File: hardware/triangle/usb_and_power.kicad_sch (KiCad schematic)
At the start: 15 parts, among them J1 USB_C_Receptacle_USB2.0_16P, J2 USB_C_Receptacle_USB2.0_16P, U2 EA8212HT6R

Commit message: trying to fix schematic
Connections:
- net -12V is gone; now on net +12V: C25.2, J1.A4 (VBUS), J1.A9 (VBUS), J1.B4 (VBUS), J1.B9 (VBUS), J2.A4 (VBUS), J2.A9 (VBUS), J2.B4 (VBUS), J2.B9 (VBUS)
- net +12V: now also C27.1, U2.5 (PWR)
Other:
- moved on the sheet: C25, C26, C27, C28, J2, L1, R3, R4, R7, R8, R9, U2

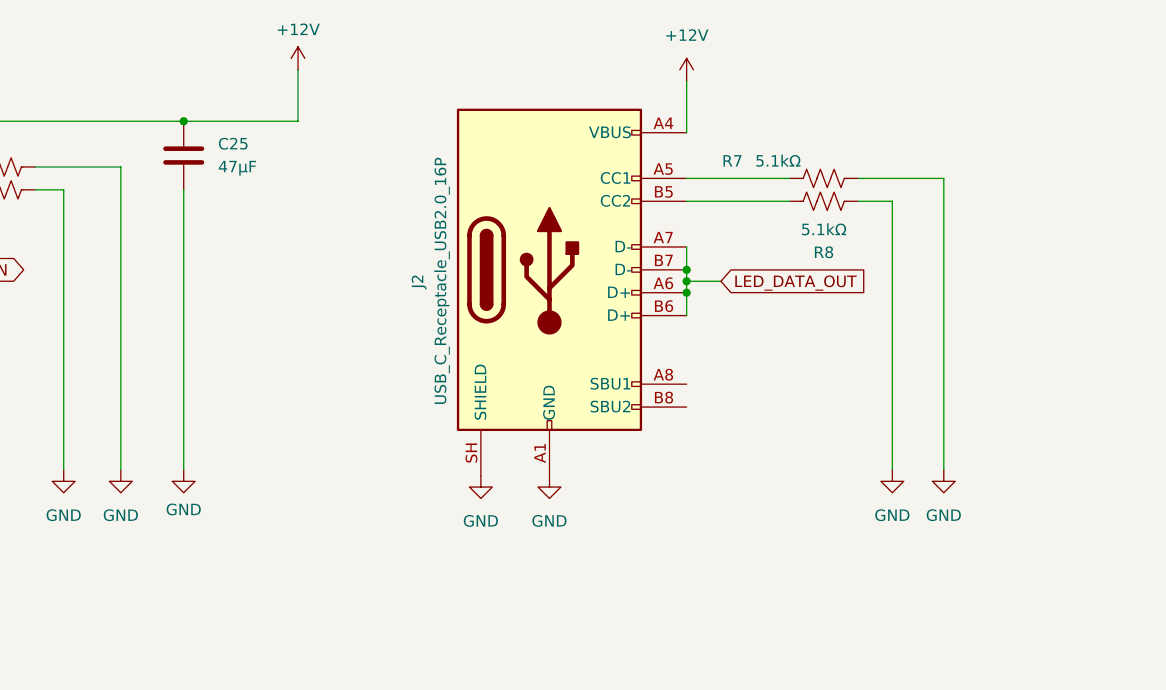
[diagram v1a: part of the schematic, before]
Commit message: add another capacitor
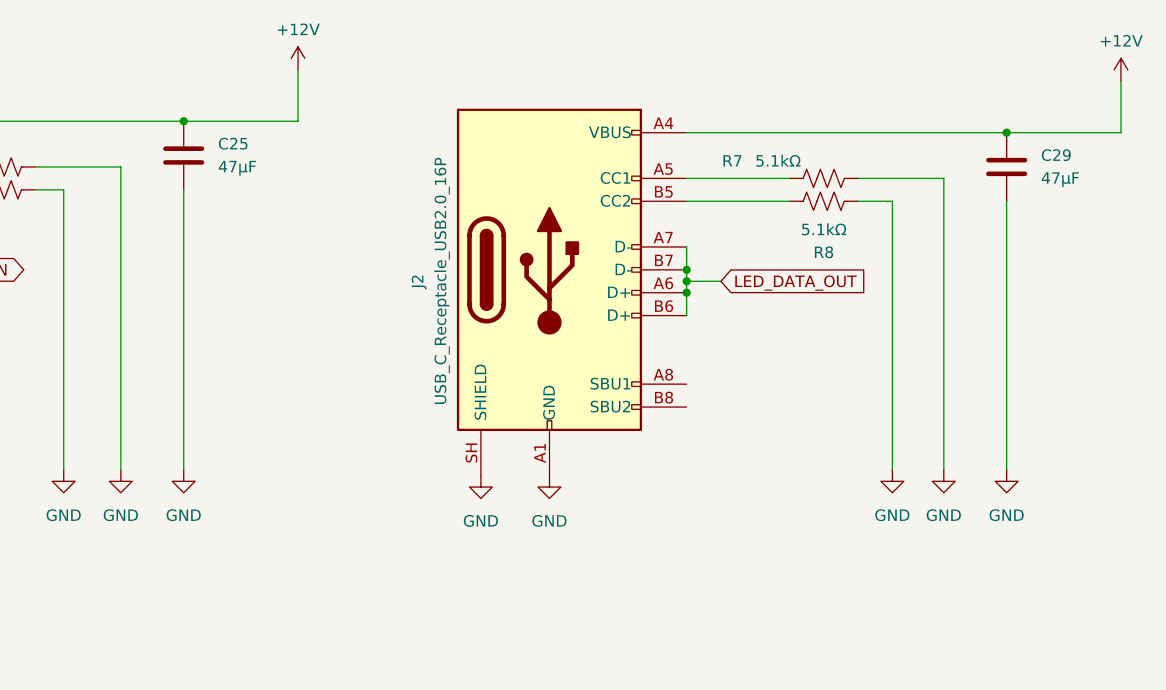
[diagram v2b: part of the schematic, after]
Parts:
- added C29: 47µF, Capacitor_SMD:C_1206_3216Metric, symbol Device:C
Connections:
- net +12V: now also C29.2
- net GND: now also C29.1
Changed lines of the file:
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@@
+	)
+	(junction
+		(at 198.12 44.45)
+		(diameter 0)
+		(color 0 0 0 0)
 	)
 	(junction
@@
 	(wire
 		(pts
+			(xy 198.12 81.915) (xy 198.12 52.07)
+		)
+		(stroke
+			(width 0)
+			(type default)
+		)
+	)
+	(wire
+		(pts
 			(xy 99.695 81.915) (xy 99.695 48.26)
 		)
@@
 	(wire
 		(pts
+			(xy 210.82 38.735) (xy 210.82 44.45)
+		)
+		(stroke
+			(width 0)
+			(type default)
+		)
+	)
+	(wire
+		(pts
 			(xy 104.775 168.91) (xy 104.775 164.465)
 		)
@@
 	(wire
 		(pts
-			(xy 162.56 44.45) (xy 162.56 38.735)
+			(xy 198.12 44.45) (xy 162.56 44.45)
 		)
 		(stroke
@@
 		(pts
 			(xy 76.835 140.97) (xy 76.835 149.86)
+		)
+		(stroke
+			(width 0)
+			(type default)
+		)
+	)
+	(wire
+		(pts
+			(xy 198.12 44.45) (xy 210.82 44.45)
 		)
 		(stroke
@@
 				)
 				(justify left)
+			)
+		)
+	)
+	(symbol
+		(lib_id "power:+12V")
+		(at 210.82 38.735 0)
+		(unit 1)
+		(body_style 1)
+		(exclude_from_sim no)
+		(in_bom yes)
+		(on_board yes)
+		(in_pos_files yes)
+		(dnp no)
+		(fields_autoplaced yes)
+		(property "Reference" "#PWR024"
+			(at 210.82 42.545 0)
+			(hide yes)
+			(show_name no)
+			(do_not_autoplace no)
+			(effects
+				(font
+					(size 1.27 1.27)
+				)
+			)
+		)
+		(property "Value" "+12V"
+			(at 210.82 34.29 0)
+			(show_name no)
+			(do_not_autoplace no)
+			(effects
+				(font
+					(size 1.27 1.27)
+				)
+			)
+		)
+		(property "Footprint" ""
+			(at 210.82 38.735 0)
+			(hide yes)
+			(show_name no)
+			(do_not_autoplace no)
+			(effects
+				(font
+					(size 1.27 1.27)
+				)
+			)
+		)
+		(property "Datasheet" ""
+			(at 210.82 38.735 0)
+			(hide yes)
+			(show_name no)
+			(do_not_autoplace no)
+			(effects
+				(font
+					(size 1.27 1.27)
+				)
+			)
+		)
+		(property "Description" "Power symbol creates a global label with name \"+12V\""
+			(at 210.82 38.735 0)
+			(hide yes)
+			(show_name no)
+			(do_not_autoplace no)
+			(effects
+				(font
+					(size 1.27 1.27)
+				)
+			)
+		)
+		(pin "1"
+		)
+		(instances
+			(project "triangle"
+				(path "/955e9dc0-fcd6-4d32-9a7f-93a0bda4c269"
+					(reference "#PWR024")
+					(unit 1)
+				)
 			)
 		)
@@
 	(symbol
 		(lib_id "power:+12V")
-		(at 162.56 38.735 0)
-		(unit 1)
-		(body_style 1)
-		(exclude_from_sim no)
-		(in_bom yes)
-		(on_board yes)
-		(in_pos_files yes)
-		(dnp no)
-		(fields_autoplaced yes)
-		(property "Reference" "#PWR016"
-			(at 162.56 42.545 0)
-			(hide yes)
-			(show_name no)
-			(do_not_autoplace no)
-			(effects
-				(font
-					(size 1.27 1.27)
-				)
-			)
-		)
-		(property "Value" "+12V"
-			(at 162.56 33.655 0)
-			(show_name no)
-			(do_not_autoplace no)
-			(effects
-				(font
-					(size 1.27 1.27)
-				)
-			)
-		)
-		(property "Footprint" ""
-			(at 162.56 38.735 0)
-			(hide yes)
-			(show_name no)
-			(do_not_autoplace no)
-			(effects
-				(font
-					(size 1.27 1.27)
-				)
-			)
-		)
-		(property "Datasheet" ""
-			(at 162.56 38.735 0)
-			(hide yes)
-			(show_name no)
-			(do_not_autoplace no)
-			(effects
-				(font
-					(size 1.27 1.27)
-				)
-			)
-		)
-		(property "Description" "Power symbol creates a global label with name \"+12V\""
-			(at 162.56 38.735 0)
-			(hide yes)
-			(show_name no)
-			(do_not_autoplace no)
-			(effects
-				(font
-					(size 1.27 1.27)
-				)
-			)
-		)
-		(pin "1"
-		)
-		(instances
-			(project "triangle"
-				(path "/955e9dc0-fcd6-4d32-9a7f-93a0bda4c269"
-					(reference "#PWR016")
-					(unit 1)
-				)
-			)
-		)
-	)
-	(symbol
-		(lib_id "power:+12V")
 		(at 142.875 113.665 0)
 		(unit 1)
@@
 	)
 	(symbol
+		(lib_id "Device:C")
+		(at 198.12 48.26 180)
+		(unit 1)
+		(body_style 1)
+		(exclude_from_sim no)
+		(in_bom yes)
+		(on_board yes)
+		(in_pos_files yes)
+		(dnp no)
+		(fields_autoplaced yes)
+		(property "Reference" "C29"
+			(at 201.93 46.9899 0)
+			(show_name no)
+			(do_not_autoplace no)
+			(effects
+				(font
+					(size 1.27 1.27)
+				)
+				(justify right)
+			)
+		)
+		(property "Value" "47µF"
+			(at 201.93 49.5299 0)
+			(show_name no)
+			(do_not_autoplace no)
+			(effects
+				(font
+					(size 1.27 1.27)
+				)
+				(justify right)
+			)
+		)
+		(property "Footprint" "Capacitor_SMD:C_1206_3216Metric"
+			(at 197.1548 44.45 0)
+			(hide yes)
+			(show_name no)
+			(do_not_autoplace no)
+			(effects
+				(font
+					(size 1.27 1.27)
+				)
+			)
+		)
+		(property "Datasheet" "https://jlc-prod-smt.oss-eu-central-1.aliyuncs.com/smtDataManualFile/8586178840691683328-C77101.pdf?response-content-disposition=attachment%3B%20filename%3DC77101.pdf%3B%20filename%2A%3DUTF-8%27%27C77101.pdf&x-oss-date=20260530T174020Z&x-oss-expires=1800&x-oss-security-token=CAISgAN1q6Ft5B2yfSjIr5n%2Bfdvem%2Bts05SjcVeCpXNkYt5rmo3Mrzz2IHhMdHJsAOodtv0%2FmmhT6PkclqRLcbhpcmfjV%2BZHzLB8qbk31zBO4J7b16cNrbH4M4H6aXeirtuwDsz9SNTCALjPD3nPii50x5bjaDymRCbLGJaViJlhHLN1Ow6jdmhpCctxLAlvo9NgFxm3D%2Fu2NQPwiWf9FVdhvhEG6Vly8qOi2MaRmFy8yFTx0b0SvJ%2BjYMrmPctoN9JnSdC5mfdzau3a1TJ84gRD0a5wkaVA1zbDs5bfISEIuUzebreLqY03dV4mOvdqIcMe8qigz88fk%2FfIioH6xyxKOexoSCnFTOiiupCcQLPyao9jLu6iayqViY7QaIOTqQohZmkAMwVOasAsI3Ngh4zF97Qt0cVNkXO9gWfLI8DtuMleWkppw9R5cnSgc5lCkRRYwGs1287ugXlSQzo890KPDAEovaKCnZ2ZSfh7Y4sNknI6i%2Bfc2Se2MIkIWjBNb6KWD5sagAGr5rmBvHeFC8TZ%2BJcd86gyYT9ErQ9X%2B0arh9aBqEUpMV00uZssw%2BpJ0wDNLR3IfY4Emrombd1Qhrr0MuB3K8fJjJk9FM3xSkdaC6wlZzPtmjTVgp5eXx0QJhMfflRGyQBUK%2FfqX4UcQ0%2FVp31Qo2ufdtTd4b5xoRPi6Re0vJceYCAA&x-oss-signature-version=OSS4-HMAC-SHA256&x-oss-credential=STS.NZK6ajv4MdVHsq3As1nQGuHgM%2F20260530%2Feu-central-1%2Foss%2Faliyun_v4_request&x-oss-signature=60c0d3c6bb64dcbae917457d6a6bcf0bef18835ea05f75f079bc953471331657"
+			(at 198.12 48.26 0)
+			(hide yes)
+			(show_name no)
+			(do_not_autoplace no)
+			(effects
+				(font
+					(size 1.27 1.27)
+				)
+			)
+		)
+		(property "Description" "Unpolarized capacitor"
+			(at 198.12 48.26 0)
+			(hide yes)
+			(show_name no)
+			(do_not_autoplace no)
+			(effects
+				(font
+					(size 1.27 1.27)
+				)
+			)
+		)
+		(property "JLCPCB Part #" "C77101"
+			(at 198.12 48.26 0)
+			(hide yes)
+			(show_name no)
+			(do_not_autoplace no)
+			(effects
+				(font
+					(size 1.27 1.27)
+				)
+			)
+		)
+		(pin "1"
+		)
+		(pin "2"
+		)
+		(instances
+			(project "triangle"
+				(path "/955e9dc0-fcd6-4d32-9a7f-93a0bda4c269"
+					(reference "C29")
+					(unit 1)
+				)
+			)
+		)
+	)
+	(symbol
 		(lib_id "Device:R_US")
 		(at 104.775 160.655 0)
@@
 		(in_pos_files yes)
 		(dnp no)
-		(fields_autoplaced yes)
 		(property "Reference" "#PWR02"
 			(at 106.68 88.265 0)
@@
 		)
 		(property "Value" "GND"
-			(at 106.68 86.36 0)
+			(at 106.68 86.995 0)
 			(show_name no)
 			(do_not_autoplace no)
@@
 					(unit 1)
 				)
+			)
+		)
+	)
+	(symbol
+		(lib_id "power:GND")
+		(at 198.12 81.915 0)
+		(unit 1)
+		(body_style 1)
+		(exclude_from_sim no)
+		(in_bom yes)
+		(on_board yes)
+		(in_pos_files yes)
+		(dnp no)
+		(property "Reference" "#PWR016"
+			(at 198.12 88.265 0)
+			(hide yes)
+			(show_name no)
+			(do_not_autoplace no)
+			(effects
+				(font
+					(size 1.27 1.27)
+				)
+			)
+		)
+		(property "Value" "GND"
+			(at 198.12 86.995 0)
+			(show_name no)
+			(do_not_autoplace no)
+			(effects
+				(font
+					(size 1.27 1.27)
+				)
+			)
+		)
+		(property "Footprint" ""
+			(at 198.12 81.915 0)
+			(hide yes)
+			(show_name no)
+			(do_not_autoplace no)
+			(effects
+				(font
+					(size 1.27 1.27)
+				)
+			)
+		)
+		(property "Datasheet" ""
+			(at 198.12 81.915 0)
+			(hide yes)
+			(show_name no)
+			(do_not_autoplace no)
+			(effects
+				(font
+					(size 1.27 1.27)
+				)
+			)
+		)
+		(property "Description" "Power symbol creates a global label with name \"GND\" , ground"
+			(at 198.12 81.915 0)
+			(hide yes)
+			(show_name no)
+			(do_not_autoplace no)
+			(effects
+				(font
+					(size 1.27 1.27)
+				)
+			)
+		)
+		(pin "1"
+		)
+		(instances
+			(project "triangle"
+				(path "/955e9dc0-fcd6-4d32-9a7f-93a0bda4c269"
+					(reference "#PWR016")
+					(unit 1)
+				)

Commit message: fix part numbering
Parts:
- C25, C29: JLCPCB Part # C77101 -> (none); LCSC Part # (none) -> C77101
- C26: JLCPCB Part # C1525 -> (none); LCSC Part # (none) -> C1525
- C27, C28: JLCPCB Part # C96446 -> (none); LCSC Part # (none) -> C96446
- J1, J2: JLCPCB # C3151749 -> (none); LCSC Part # (none) -> C3151749
- L1: JLCPCB # C281115 -> (none); LCSC Part # (none) -> C281115
- R3, R9: JLCPCB # C60491 -> (none); LCSC Part # (none) -> C60491
- R4: JLCPCB # C132339 -> (none); LCSC Part # (none) -> C132339
- R5, R6, R7, R8: JLCPCB Part # C23186 -> (none); LCSC Part # (none) -> C23186
- U2: JLCPCB # C609568 -> (none); LCSC Part # (none) -> C609568
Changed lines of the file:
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@@
 			)
 		)
-		(property "JLCPCB #" "C3151749"
+		(property "LCSC Part #" "C3151749"
 			(at 147.32 59.69 90)
 			(hide yes)
@@
 			)
 		)
-		(property "JLCPCB #" "C3151749"
+		(property "LCSC Part #" "C3151749"
 			(at 55.88 58.42 90)
 			(hide yes)
@@
 			)
 		)
-		(property "JLCPCB Part #" "C96446"
+		(property "LCSC Part #" "C96446"
 			(at 121.92 137.16 90)
 			(hide yes)
@@
 			)
 		)
-		(property "JLCPCB Part #" "C23186"
+		(property "LCSC Part #" "C23186"
 			(at 177.8 49.53 90)
 			(hide yes)
@@
 			)
 		)
-		(property "JLCPCB Part #" "C77101"
+		(property "LCSC Part #" "C77101"
 			(at 198.12 48.26 0)
 			(hide yes)
@@
 			)
 		)
-		(property "JLCPCB #" "C60491"
+		(property "LCSC Part #" "C60491"
 			(at 104.775 160.655 0)
 			(hide yes)
@@
 			)
 		)
-		(property "JLCPCB #" "C609568"
+		(property "LCSC Part #" "C609568"
 			(at 89.535 172.72 0)
 			(hide yes)
@@
 			)
 		)
-		(property "JLCPCB #" "C60491"
+		(property "LCSC Part #" "C60491"
 			(at 53.975 170.18 0)
 			(hide yes)
@@
 			)
 		)
-		(property "JLCPCB Part #" "C23186"
+		(property "LCSC Part #" "C23186"
 			(at 86.36 50.8 90)
 			(hide yes)
@@
 			)
 		)
-		(property "JLCPCB Part #" "C77101"
+		(property "LCSC Part #" "C77101"
 			(at 106.68 46.99 0)
 			(hide yes)
@@
 			)
 		)
-		(property "JLCPCB Part #" "C23186"
+		(property "LCSC Part #" "C23186"
 			(at 86.36 48.26 90)
 			(hide yes)
@@
 			)
 		)
-		(property "JLCPCB Part #" "C96446"
+		(property "LCSC Part #" "C96446"
 			(at 130.175 156.21 90)
 			(hide yes)
@@
 			)
 		)
-		(property "JLCPCB #" "C281115"
+		(property "LCSC Part #" "C281115"
 			(at 111.125 151.13 0)
 			(hide yes)
@@
 			)
 		)
-		(property "JLCPCB #" "C132339"
+		(property "LCSC Part #" "C132339"
 			(at 62.865 166.37 0)
 			(hide yes)
@@
 			)
 		)
-		(property "LCSC Part Number" ""
-			(at 76.835 137.16 0)
-			(hide yes)
-			(show_name no)
-			(do_not_autoplace no)
-			(effects
-				(font
-					(size 1.27 1.27)
-				)
-			)
-		)
-		(property "JLCPCB Part #" "C1525"
+		(property "LCSC Part #" "C1525"
 			(at 76.835 137.16 0)
 			(hide yes)
@@
 			)
 		)
-		(property "JLCPCB Part #" "C23186"
+		(property "LCSC Part #" "C23186"
 			(at 177.8 52.07 90)
 			(hide yes)
